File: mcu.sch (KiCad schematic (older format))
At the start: 40 parts

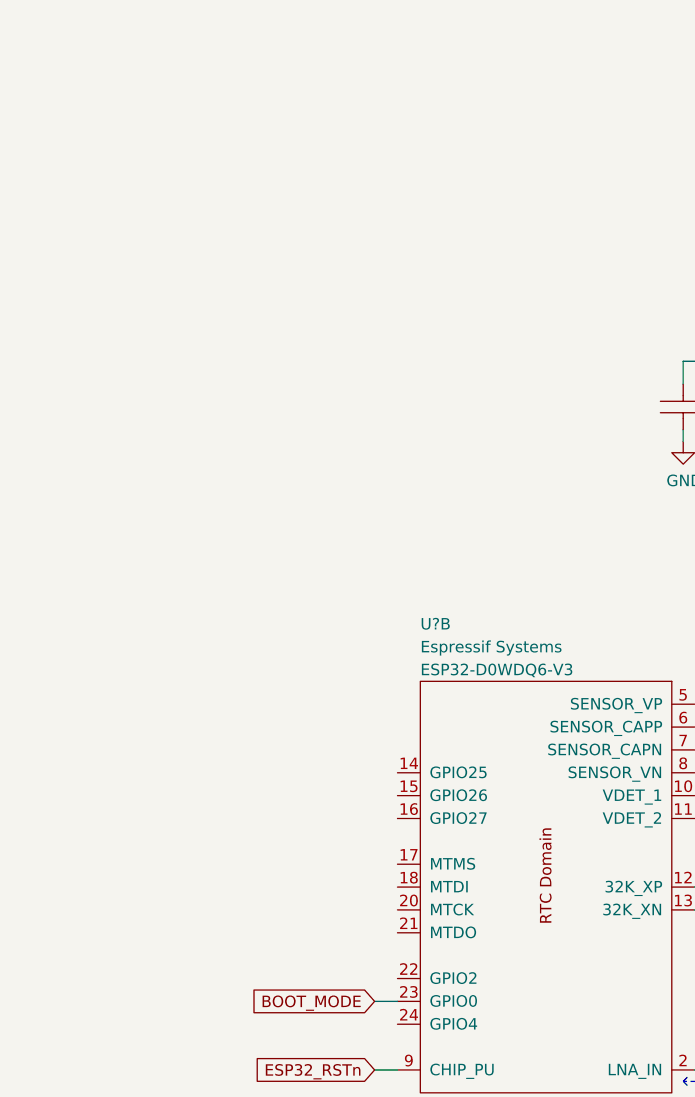
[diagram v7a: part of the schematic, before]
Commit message: Add JTAG interface.
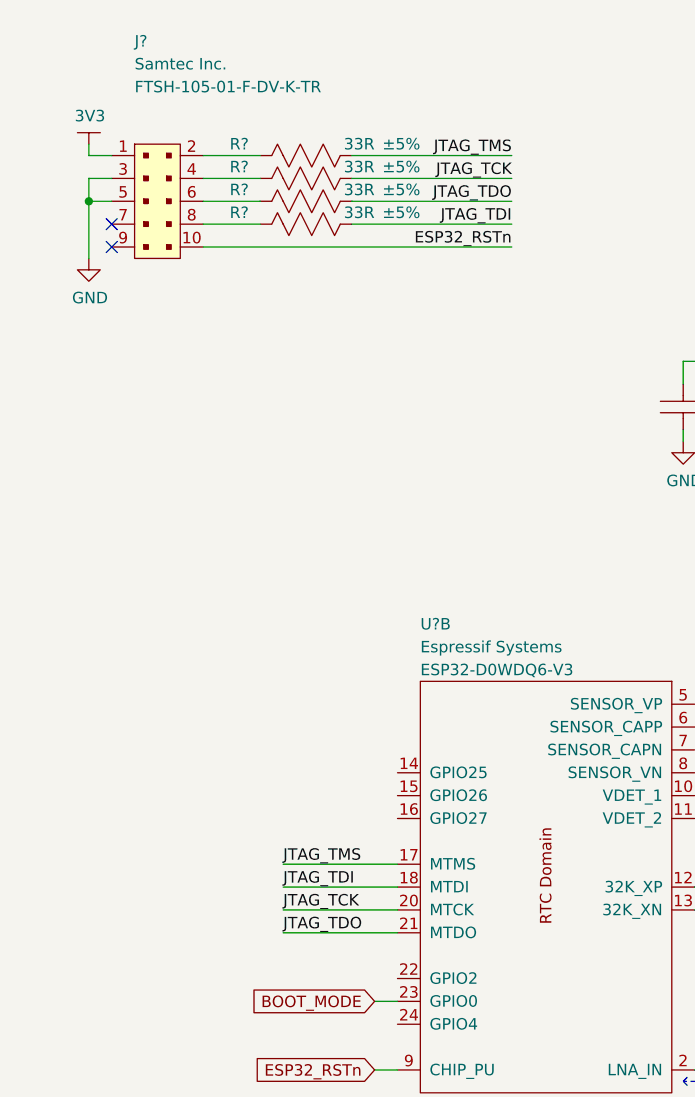
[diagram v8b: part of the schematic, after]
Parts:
- added J?: Samtec-FTSH-105-01-F-DV-K-TR, footprints:Samtec_FTSH-105-01-F-DV-K-TR, symbol gz_Rectangular-Connectors-Headers-Male-Pins:Samtec-FTSH-105-01-F-DV-K-TR
- added R? (x4): RES-EIA0402, footprints_generic:RESC100X50X40L25NN, symbol gz_Chip-Resistors-Surface-Mount:RES-EIA0402
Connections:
- net +3V3: now also J?.1
- net ESP32_RSTn: now also J?.10
- net GND: now also J?.3, J?.5
- net JTAG_TMS: now reaches U?.17 (MTMS)
- net JTAG_TMS: now also R?.1
- net JTAG_TDI: now reaches U?.18 (MTDI)
- net JTAG_TDI: now also R?.1
- net JTAG_TCK: now reaches U?.20 (MTCK)
- net JTAG_TCK: now also R?.1
- net JTAG_TDO: now reaches U?.21 (MTDO)
- net JTAG_TDO: now also R?.1
- new net: J?.2, R?.2
- new net: J?.4, R?.2
- new net: J?.6, R?.2
- new net: J?.8, R?.2
- no-connect marks 0 -> 2
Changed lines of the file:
@@
 Text GLabel 2200 4950 0    50   Input ~ 0
 BOOT_MODE
+$Comp
+L gz_Rectangular-Connectors-Headers-Male-Pins:Samtec-FTSH-105-01-F-DV-K-TR J?
+U 1 1 6079BF3E
+P 1250 1450
+F 0 "J?" H 1150 2150 50  0000 L CNN
+F 1 "Samtec-FTSH-105-01-F-DV-K-TR" H 1750 2300 50  0001 L CNN
+F 2 "footprints:Samtec_FTSH-105-01-F-DV-K-TR" H 1750 2400 50  0001 L CNN
+F 3 "${DATASHEETS}/Samtec_FTSH-SMT.pdf" H 2050 150 50  0001 L CNN
+F 4 "Digikey" H 1750 2200 50  0001 L CNN "Vendor"
+F 5 "SAM13160CT-ND" H 2050 2200 50  0001 L CNN "Vendor_PN"
+F 6 "Samtec Inc." H 1150 2050 50  0000 L CNN "Manufacturer"
+F 7 "FTSH-105-01-F-DV-K-TR" H 1150 1950 50  0000 L CNN "MPN"
+F 8 "Connectors, Interconnects" H 1750 2100 50  0001 L CNN "Category"
+F 9 "Rectangular Connectors - Headers, Male Pins" H 1750 2000 50  0001 L CNN "Family"
+F 10 "Yes" H 1300 1900 50  0001 L CNN "Fit"
+	1    1250 1450
+	1    0    0    -1
+$EndComp
+Wire Wire Line
+	1050 1350 950  1350
+Wire Wire Line
+	950  1350 950  1450
+Wire Wire Line
+	1050 1450 950  1450
+Connection ~ 950  1450
+Wire Wire Line
+	950  1450 950  1700
+Wire Wire Line
+	1050 1250 950  1250
+Wire Wire Line
+	950  1250 950  1200
+$Comp
+L gz_Power-Symbols:3V3 #PWR?
+U 1 1 607B6F1E
+P 950 1200
+F 0 "#PWR?" H 1100 1150 50  0001 C CNN
+F 1 "3V3" H 955 1323 50  0000 C CNN
+F 2 "" H 950 1200 50  0001 C CNN
+F 3 "" H 950 1200 50  0001 C CNN
+	1    950  1200
+	1    0    0    -1
+$EndComp
+Wire Wire Line
+	2300 4350 1800 4350
+Wire Wire Line
+	2300 4450 1800 4450
+Wire Wire Line
+	2300 4550 1800 4550
+Wire Wire Line
+	2300 4650 1800 4650
+Text Label 1800 4350 0    50   ~ 0
+JTAG_TMS
+Text Label 1800 4650 0    50   ~ 0
+JTAG_TDO
+Text Label 1800 4450 0    50   ~ 0
+JTAG_TDI
+Text Label 1800 4550 0    50   ~ 0
+JTAG_TCK
+Wire Wire Line
+	2100 1250 2800 1250
+Wire Wire Line
+	2100 1550 2800 1550
+Wire Wire Line
+	2100 1350 2800 1350
+Wire Wire Line
+	2100 1450 2800 1450
+Text Label 2800 1250 2    50   ~ 0
+JTAG_TMS
+Text Label 2800 1450 2    50   ~ 0
+JTAG_TDO
+Text Label 2800 1550 2    50   ~ 0
+JTAG_TDI
+Text Label 2800 1350 2    50   ~ 0
+JTAG_TCK
+$Comp
+L gz_Chip-Resistors-Surface-Mount:RES-EIA0402 R?
+U 1 1 6082CA10
+P 1900 1350
+AR Path="/60330427/6082CA10" Ref="R?"  Part="1"
+AR Path="/606CDE66/6082CA10" Ref="R?"  Part="1"
+F 0 "R?" H 2150 1300 50  0000 L CNN
+F 1 "RES-EIA0402" H 2700 2250 50  0001 L CNN
+F 2 "footprints_generic:RESC100X50X40L25NN" H -1400 5700 50  0001 L CNN
+F 3 "${PANASONIC_GP_CHIP_RES_BASE}ERJ2GEJ330X" H -1400 5800 50  0001 L CNN
+F 4 "Digikey" H 1900 1350 50  0001 L CNN "Vendor"
+F 5 "P33KJCT-ND" H 1900 1350 50  0001 L CNN "Vendor_PN"
+F 6 "Panasonic Electronic Components" H 2700 2050 50  0001 L CNN "Manufacturer"
+F 7 "ERJ2GEJ330X" H 2700 1950 50  0001 L CNN "MPN"
+F 8 "Resistors" H -1400 6100 50  0001 L CNN "Category"
+F 9 "Chip Resistor - Surface Mount" H -1400 6200 50  0001 L CNN "Family"
+F 10 "Yes" H 1900 1350 50  0001 C CNN "Fit"
+F 11 "33R" H 1600 1300 50  0000 L CNN "Resistance"
+F 12 "±5%" H 1400 1300 50  0000 L CNN "Tolerance"
+F 13 "1/10W" H 2050 1400 50  0001 L CNN "Power"
+F 14 "N/A" H 1900 1565 50  0001 L CNN "Voltage"
+F 15 "EIA0402" H 1450 1400 50  0001 L CNN "Package"
+	1    1900 1350
+	-1   0    0    1
+$EndComp
+$Comp
+L gz_Chip-Resistors-Surface-Mount:RES-EIA0402 R?
+U 1 1 6085CDA5
+P 1900 1450
+AR Path="/60330427/6085CDA5" Ref="R?"  Part="1"
+AR Path="/606CDE66/6085CDA5" Ref="R?"  Part="1"
+F 0 "R?" H 2150 1400 50  0000 L CNN
+F 1 "RES-EIA0402" H 2700 2350 50  0001 L CNN
+F 2 "footprints_generic:RESC100X50X40L25NN" H -1400 5800 50  0001 L CNN
+F 3 "${PANASONIC_GP_CHIP_RES_BASE}ERJ2GEJ330X" H -1400 5900 50  0001 L CNN
+F 4 "Digikey" H 1900 1450 50  0001 L CNN "Vendor"
+F 5 "P33KJCT-ND" H 1900 1450 50  0001 L CNN "Vendor_PN"
+F 6 "Panasonic Electronic Components" H 2700 2150 50  0001 L CNN "Manufacturer"
+F 7 "ERJ2GEJ330X" H 2700 2050 50  0001 L CNN "MPN"
+F 8 "Resistors" H -1400 6200 50  0001 L CNN "Category"
+F 9 "Chip Resistor - Surface Mount" H -1400 6300 50  0001 L CNN "Family"
+F 10 "Yes" H 1900 1450 50  0001 C CNN "Fit"
+F 11 "33R" H 1600 1400 50  0000 L CNN "Resistance"
+F 12 "±5%" H 1400 1400 50  0000 L CNN "Tolerance"
+F 13 "1/10W" H 2050 1500 50  0001 L CNN "Power"
+F 14 "N/A" H 1900 1665 50  0001 L CNN "Voltage"
+F 15 "EIA0402" H 1450 1500 50  0001 L CNN "Package"
+	1    1900 1450
+	-1   0    0    1
+$EndComp
+$Comp
+L gz_Chip-Resistors-Surface-Mount:RES-EIA0402 R?
+U 1 1 6085D372
+P 1900 1550
+AR Path="/60330427/6085D372" Ref="R?"  Part="1"
+AR Path="/606CDE66/6085D372" Ref="R?"  Part="1"
+F 0 "R?" H 2150 1500 50  0000 L CNN
+F 1 "RES-EIA0402" H 2700 2450 50  0001 L CNN
+F 2 "footprints_generic:RESC100X50X40L25NN" H -1400 5900 50  0001 L CNN
+F 3 "${PANASONIC_GP_CHIP_RES_BASE}ERJ2GEJ330X" H -1400 6000 50  0001 L CNN
+F 4 "Digikey" H 1900 1550 50  0001 L CNN "Vendor"
+F 5 "P33KJCT-ND" H 1900 1550 50  0001 L CNN "Vendor_PN"
+F 6 "Panasonic Electronic Components" H 2700 2250 50  0001 L CNN "Manufacturer"
+F 7 "ERJ2GEJ330X" H 2700 2150 50  0001 L CNN "MPN"
+F 8 "Resistors" H -1400 6300 50  0001 L CNN "Category"
+F 9 "Chip Resistor - Surface Mount" H -1400 6400 50  0001 L CNN "Family"
+F 10 "Yes" H 1900 1550 50  0001 C CNN "Fit"
+F 11 "33R" H 1600 1500 50  0000 L CNN "Resistance"
+F 12 "±5%" H 1400 1500 50  0000 L CNN "Tolerance"
+F 13 "1/10W" H 2050 1600 50  0001 L CNN "Power"
+F 14 "N/A" H 1900 1765 50  0001 L CNN "Voltage"
+F 15 "EIA0402" H 1450 1600 50  0001 L CNN "Package"
+	1    1900 1550
+	-1   0    0    1
+$EndComp
+$Comp
+L gz_Chip-Resistors-Surface-Mount:RES-EIA0402 R?
+U 1 1 6085D8AE
+P 1900 1250
+AR Path="/60330427/6085D8AE" Ref="R?"  Part="1"
+AR Path="/606CDE66/6085D8AE" Ref="R?"  Part="1"
+F 0 "R?" H 2150 1200 50  0000 L CNN
+F 1 "RES-EIA0402" H 2700 2150 50  0001 L CNN
+F 2 "footprints_generic:RESC100X50X40L25NN" H -1400 5600 50  0001 L CNN
+F 3 "${PANASONIC_GP_CHIP_RES_BASE}ERJ2GEJ330X" H -1400 5700 50  0001 L CNN
+F 4 "Digikey" H 1900 1250 50  0001 L CNN "Vendor"
+F 5 "P33KJCT-ND" H 1900 1250 50  0001 L CNN "Vendor_PN"
+F 6 "Panasonic Electronic Components" H 2700 1950 50  0001 L CNN "Manufacturer"
+F 7 "ERJ2GEJ330X" H 2700 1850 50  0001 L CNN "MPN"
+F 8 "Resistors" H -1400 6000 50  0001 L CNN "Category"
+F 9 "Chip Resistor - Surface Mount" H -1400 6100 50  0001 L CNN "Family"
+F 10 "Yes" H 1900 1250 50  0001 C CNN "Fit"
+F 11 "33R" H 1600 1200 50  0000 L CNN "Resistance"
+F 12 "±5%" H 1400 1200 50  0000 L CNN "Tolerance"
+F 13 "1/10W" H 2050 1300 50  0001 L CNN "Power"
+F 14 "N/A" H 1900 1465 50  0001 L CNN "Voltage"
+F 15 "EIA0402" H 1450 1300 50  0001 L CNN "Package"
+	1    1900 1250
+	-1   0    0    1
+$EndComp
+Wire Wire Line
+	1450 1250 1700 1250
+Wire Wire Line
+	1700 1350 1450 1350
+Wire Wire Line
+	1700 1450 1450 1450
+Wire Wire Line
+	1450 1550 1700 1550
+$Comp
+L gz_Power-Symbols:GND #PWR?
+U 1 1 608E3B60
+P 950 1700
+F 0 "#PWR?" H 950 1450 50  0001 C CNN
+F 1 "GND" H 955 1527 50  0000 C CNN
+F 2 "" H 950 1700 50  0001 C CNN
+F 3 "" H 950 1700 50  0001 C CNN
+	1    950  1700
+	1    0    0    -1
+$EndComp
+NoConn ~ 1050 1550
+NoConn ~ 1050 1650
+Wire Wire Line
+	1450 1650 2800 1650
+Text Label 2800 1650 2    50   ~ 0
+ESP32_RSTn
 $EndSCHEMATC
